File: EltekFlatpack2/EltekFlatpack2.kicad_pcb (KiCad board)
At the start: 2 copper layers, 26.2 x 81 mm, 14 parts

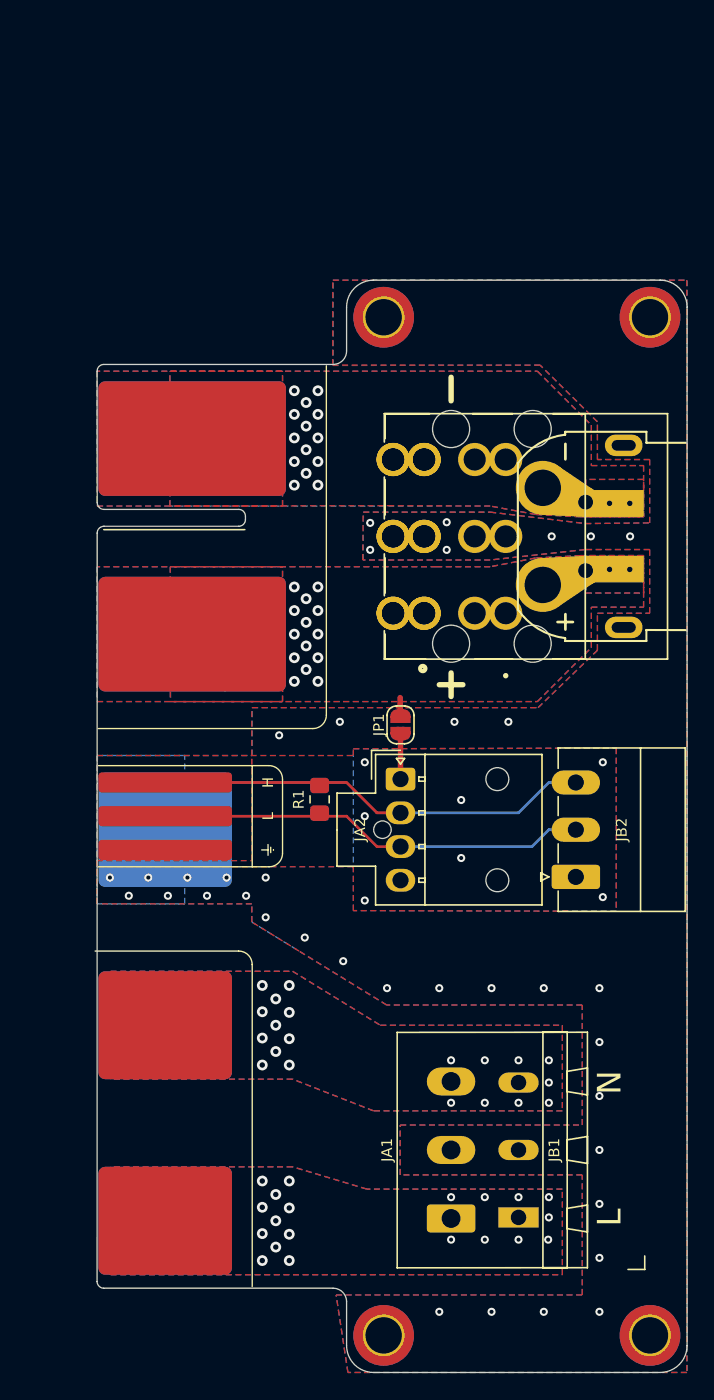
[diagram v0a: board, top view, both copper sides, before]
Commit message: fix makefile/panel/footprint (now has 1mm mill hole and straight edges!)
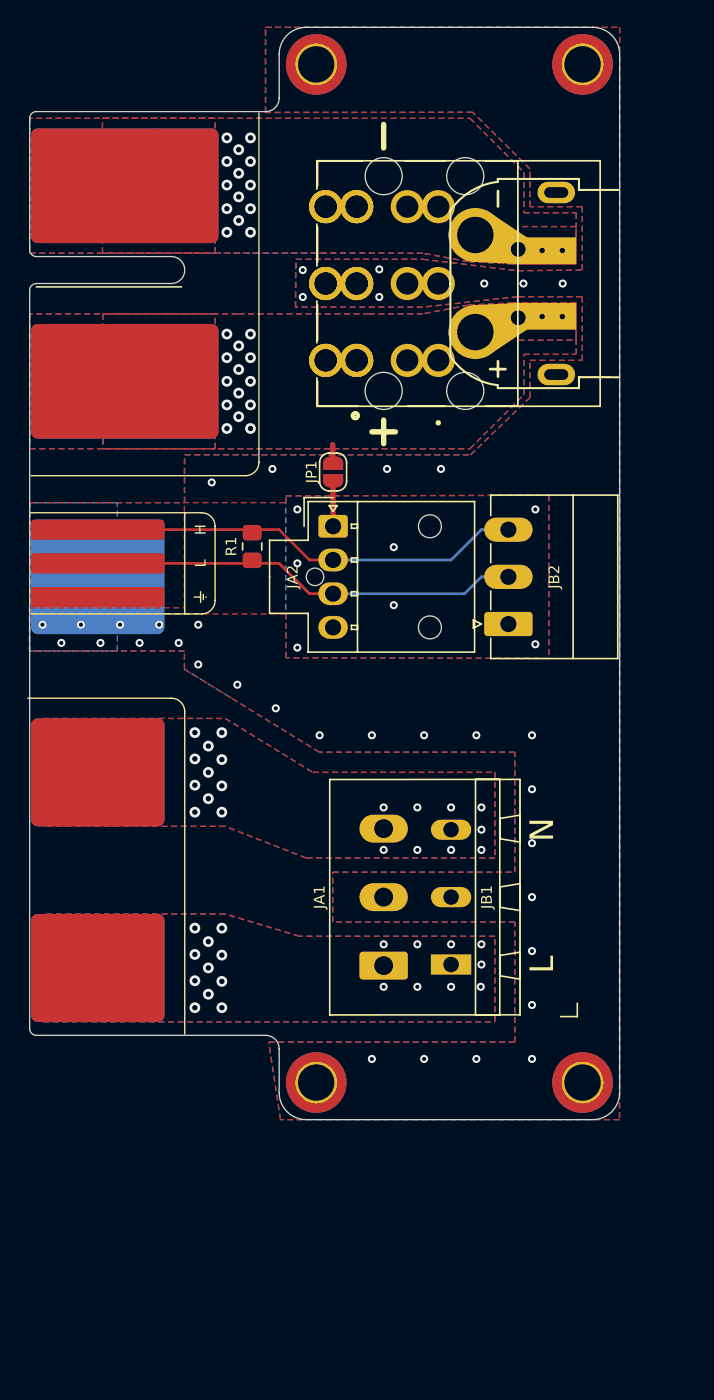
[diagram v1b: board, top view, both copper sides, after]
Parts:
- moved JA1 19.4 mm to (146.2, 119.6)
- moved H1 19.4 mm to (141.2, 128.2)
- moved H2 19.4 mm to (161.0, 128.2)
- moved H3 19.4 mm to (141.2, 52.8)
- moved H4 19.4 mm to (161.0, 52.8)
- moved JA2 19.4 mm to (142.5, 87.0)
- moved JA3 19.4 mm to (146.2, 69.0)
- moved JB1 19.4 mm to (151.2, 119.5)
- moved JB2 19.4 mm to (155.5, 94.2)
- moved JB3 19.4 mm to (152.3, 69.0)
- moved JC3 19.4 mm to (153.1, 69.0)
- moved JP1 19.4 mm to (142.5, 83.0)
- moved PC1 19.4 mm to (120.0, 56.2)
- moved R1 19.4 mm to (136.5, 88.5)
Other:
- board text removed: "appx 325mm to front of PSU"

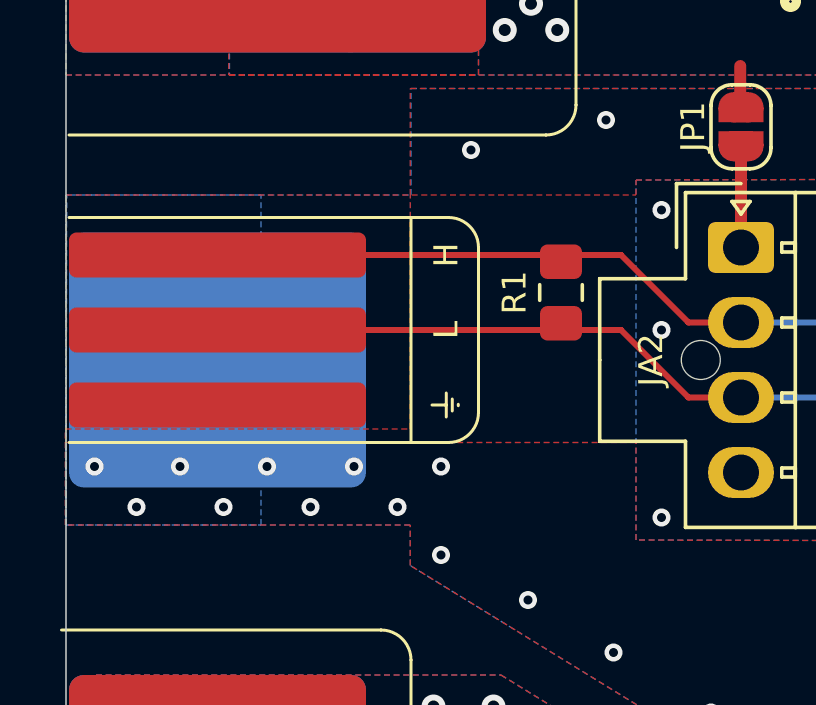
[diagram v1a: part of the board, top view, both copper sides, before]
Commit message: add THT termination resistor option
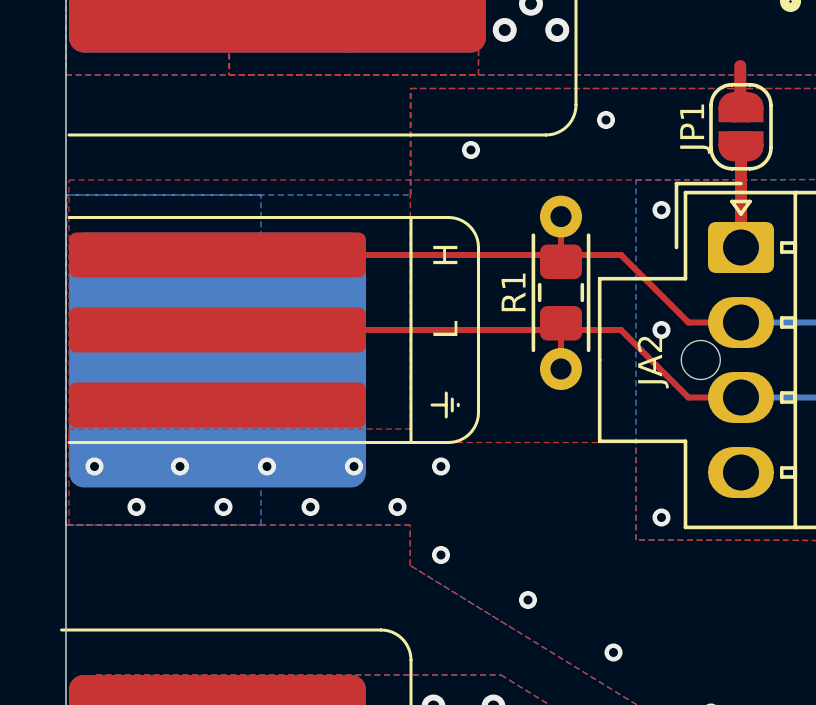
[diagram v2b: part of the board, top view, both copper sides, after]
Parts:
- added R2: 120R, Resistor_THT:R_Axial_DIN0204_L3.6mm_D1.6mm_P5.08mm_Horizontal, F.Cu at (136.5, 91.0)
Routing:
- net /CAN-: track 32.1 -> 33.7 mm
- net /CAN+: track 32.6 -> 34.1 mm
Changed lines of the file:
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@@
     (thickness 1.6)
     (drawings 32)
-    (tracks 140)
+    (tracks 142)
     (zones 0)
-    (modules 14)
+    (modules 15)
     (nets 10)
   )
@@
   )
   (setup
-    (last_trace_width 0.15)
+    (last_trace_width 0.2)
     (user_trace_width 0.15)
     (user_trace_width 0.2)
@@
     (add_net GNDD)
   )
+  (module Resistor_THT:R_Axial_DIN0204_L3.6mm_D1.6mm_P5.08mm_Horizontal (layer Front)
+    (at 136.5 91.05 90)
+    (descr "Resistor, Axial_DIN0204 series, Axial, Horizontal, pin pitch=5.08mm, 0.167W, length*diameter=3.6*1.6mm^2, http://cdn-reichelt.de/documents/datenblatt/B400/1_4W%23YAG.pdf")
+    (tags "Resistor Axial_DIN0204 series Axial Horizontal pin pitch 5.08mm 0.167W length 3.6mm diameter 1.6mm")
+    (fp_text reference R2 (at 2.54 -1.92 90) (layer F.SilkS) hide
+      (effects (font (size 1 1) (thickness 0.15)))
+    )
+    (fp_text value 120R (at 2.54 1.92 90) (layer F.Fab)
+      (effects (font (size 1 1) (thickness 0.15)))
+    )
+    (fp_line (start 6.03 -1.05) (end -0.95 -1.05) (layer F.CrtYd) (width 0.05))
+    (fp_line (start 6.03 1.05) (end 6.03 -1.05) (layer F.CrtYd) (width 0.05))
+    (fp_line (start -0.95 1.05) (end 6.03 1.05) (layer F.CrtYd) (width 0.05))
+    (fp_line (start -0.95 -1.05) (end -0.95 1.05) (layer F.CrtYd) (width 0.05))
+    (fp_line (start 0.62 0.92) (end 4.46 0.92) (layer F.SilkS) (width 0.12))
+    (fp_line (start 0.62 -0.92) (end 4.46 -0.92) (layer F.SilkS) (width 0.12))
+    (fp_line (start 5.08 0) (end 4.34 0) (layer F.Fab) (width 0.1))
+    (fp_line (start 0 0) (end 0.74 0) (layer F.Fab) (width 0.1))
+    (fp_line (start 4.34 -0.8) (end 0.74 -0.8) (layer F.Fab) (width 0.1))
+    (fp_line (start 4.34 0.8) (end 4.34 -0.8) (layer F.Fab) (width 0.1))
+    (fp_line (start 0.74 0.8) (end 4.34 0.8) (layer F.Fab) (width 0.1))
+    (fp_line (start 0.74 -0.8) (end 0.74 0.8) (layer F.Fab) (width 0.1))
+    (fp_text user %R (at 2.54 0 90) (layer F.Fab)
+      (effects (font (size 0.72 0.72) (thickness 0.108)))
+    )
+    (pad 2 thru_hole oval (at 5.08 0 90) (size 1.4 1.4) (drill 0.7) (layers *.Cu *.Mask)
+      (net 2 /CAN+))
+    (pad 1 thru_hole circle (at 0 0 90) (size 1.4 1.4) (drill 0.7) (layers *.Cu *.Mask)
+      (net 1 /CAN-))
+    (model ${KISYS3DMOD}/Resistor_THT.3dshapes/R_Axial_DIN0204_L3.6mm_D1.6mm_P5.08mm_Horizontal.wrl
+      (at (xyz 0 0 0))
+      (scale (xyz 1 1 1))
+      (rotate (xyz 0 0 0))
+    )
+  )
   (module EltekFlatpack2:CON_Edge_Flatpack2_AllContacts locked (layer Front)
     (at 120 56.25)
@@
       (effects (font (size 0.8 0.8) (thickness 0.12)))
     )
-    (fp_arc (start 10.5 11.75) (end 10.5 12.75) (angle -180) (layer Edge.Cuts) (width 0.05))
-    (fp_arc (start 0.5 13.25) (end 0.5 12.75) (angle -90) (layer Edge.Cuts) (width 0.05))
-    (fp_text user L (at 12.675 33.5 90 unlocked) (layer F.SilkS)
-      (effects (font (size 0.8 0.8) (thickness 0.12)))
-    )
-    (fp_arc (start 0.5 0.5) (end 0.5 0) (angle -90) (layer Edge.Cuts) (width 0.05))
-    (fp_arc (start 0.5 10.25) (end 0 10.25) (angle -90) (layer Edge.Cuts) (width 0.05))
-    (fp_arc (start 0.5 68) (end 0 68) (angle -90) (layer Edge.Cuts) (width 0.05))
-    (fp_arc (start 0.5 68) (end 0 68) (angle -90) (layer F.CrtYd) (width 0.05))
-    (fp_arc (start 0.5 0.5) (end 0.5 0) (angle -90) (layer F.CrtYd) (width 0.05))
-    (fp_arc (start 16 26) (end 16 27) (angle -90) (layer F.SilkS) (width 0.1))
-    (fp_text user H (at 12.675 31 90 unlocked) (layer F.SilkS)
-      (effects (font (size 0.8 0.8) (thickness 0.12)))
-    )
-    (fp_arc (start 12.75 30.75) (end 13.75 30.75) (angle -90) (layer F.SilkS) (width 0.1))
-    (fp_arc (start 12.75 36.25) (end 12.75 37.25) (angle -90) (layer F.SilkS) (width 0.1))
-    (fp_arc (start 10.5 44.5) (end 11.5 44.5) (angle -90) (layer F.SilkS) (width 0.1))
     (fp_line (start 13.75 30.75) (end 13.75 36.25) (layer F.SilkS) (width 0.1))
     (fp_line (start 0.1 37.25) (end 12.75 37.25) (layer F.SilkS) (width 0.1))
@@
     (fp_line (start 12.875 36.2) (end 12.875 35.8) (layer F.SilkS) (width 0.1))
     (fp_line (start 11.25 13) (end 0.5 13) (layer F.SilkS) (width 0.12))
+    (fp_arc (start 10.5 11.75) (end 10.5 12.75) (angle -180) (layer Edge.Cuts) (width 0.05))
+    (fp_arc (start 0.5 13.25) (end 0.5 12.75) (angle -90) (layer Edge.Cuts) (width 0.05))
+    (fp_text user L (at 12.675 33.5 90 unlocked) (layer F.SilkS)
+      (effects (font (size 0.8 0.8) (thickness 0.12)))
+    )
+    (fp_arc (start 0.5 0.5) (end 0.5 0) (angle -90) (layer Edge.Cuts) (width 0.05))
+    (fp_arc (start 0.5 10.25) (end 0 10.25) (angle -90) (layer Edge.Cuts) (width 0.05))
+    (fp_arc (start 0.5 68) (end 0 68) (angle -90) (layer Edge.Cuts) (width 0.05))
+    (fp_arc (start 0.5 68) (end 0 68) (angle -90) (layer F.CrtYd) (width 0.05))
+    (fp_arc (start 0.5 0.5) (end 0.5 0) (angle -90) (layer F.CrtYd) (width 0.05))
+    (fp_arc (start 16 26) (end 16 27) (angle -90) (layer F.SilkS) (width 0.1))
+    (fp_text user H (at 12.675 31 90 unlocked) (layer F.SilkS)
+      (effects (font (size 0.8 0.8) (thickness 0.12)))
+    )
+    (fp_arc (start 12.75 30.75) (end 13.75 30.75) (angle -90) (layer F.SilkS) (width 0.1))
+    (fp_arc (start 12.75 36.25) (end 12.75 37.25) (angle -90) (layer F.SilkS) (width 0.1))
+    (fp_arc (start 10.5 44.5) (end 11.5 44.5) (angle -90) (layer F.SilkS) (width 0.1))
     (pad CAN-L smd roundrect (at 5.05 33.5) (size 9.9 1.5) (layers Front F.Mask) (roundrect_rratio 0.167)
       (net 1 /CAN-) (solder_mask_margin 0.1016))
@@
   (segment (start 138.5 89.75) (end 140.75 92) (width 0.2) (layer Front) (net 1))
   (segment (start 136.45 89.75) (end 138.5 89.75) (width 0.2) (layer Front) (net 1))
+  (segment (start 136.5 89.525) (end 136.5 91.05) (width 0.2) (layer Front) (net 1))
   (segment (start 136.5 87.3) (end 136.55 87.25) (width 0.154) (layer Front) (net 2))
   (segment (start 136.5 87.475) (end 136.5 87.3) (width 0.154) (layer Front) (net 2))
@@
   (segment (start 151.25 89.5) (end 153.5 87.25) (width 0.2) (layer Back) (net 2))
   (segment (start 142.5 89.5) (end 151.25 89.5) (width 0.2) (layer Back) (net 2))
+  (segment (start 136.5 87.475) (end 136.5 85.97) (width 0.2) (layer Front) (net 2))
   (via (at 157.5 85.75) (size 0.6) (drill 0.3) (layers Front Back) (net 3))
   (via (at 157.5 95.75) (size 0.6) (drill 0.3) (layers Front Back) (net 3))
@@
         (xy 163.725 131) (xy 138.6 131) (xy 137.725 125.25) (xy 155.975 125.25) (xy 155.975 116.35)
         (xy 142.475 116.35) (xy 142.475 112.65) (xy 155.975 112.65) (xy 155.975 103.75) (xy 141.475 103.75)
-        (xy 134.975 99.75) (xy 131.475 97.6) (xy 131.475 96.25) (xy 119.975 96.25) (xy 119.975 93.05)
+        (xy 134.975 99.75) (xy 131.475 97.6) (xy 131.475 96.25) (xy 120.1 96.25) (xy 120.1 93.05)
         (xy 131.475 93.05) (xy 131.475 85.25) (xy 131.475 81.7) (xy 152.7 81.7) (xy 157.1 77.45)
         (xy 157.1 74.7) (xy 160.975 74.7) (xy 160.975 69.975) (xy 156.2 69.975) (xy 149.15 70.75)
@@
     (polygon
       (pts
-        (xy 158.5 96.8) (xy 139 96.75) (xy 139 93.5) (xy 120 93.5) (xy 120 85.25)
-        (xy 139 85.25) (xy 139 84.75) (xy 158.5 84.7)
-      )
-    )
+        (xy 158.5 96.8) (xy 139 96.75) (xy 139 93.5) (xy 120.1 93.5) (xy 120.1 84.75)
+        (xy 139 84.75) (xy 158.5 84.7)
+      )
+    )

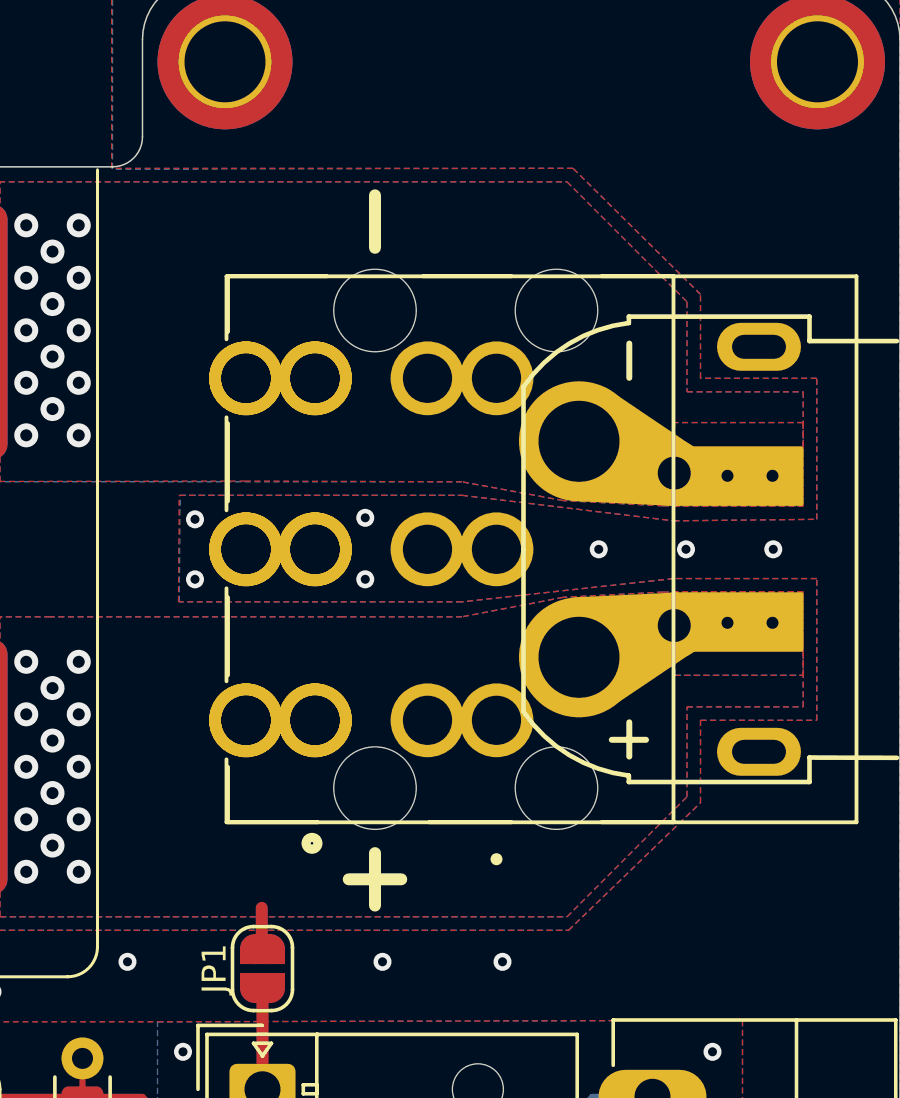
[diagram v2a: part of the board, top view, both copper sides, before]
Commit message: add keystone tab option
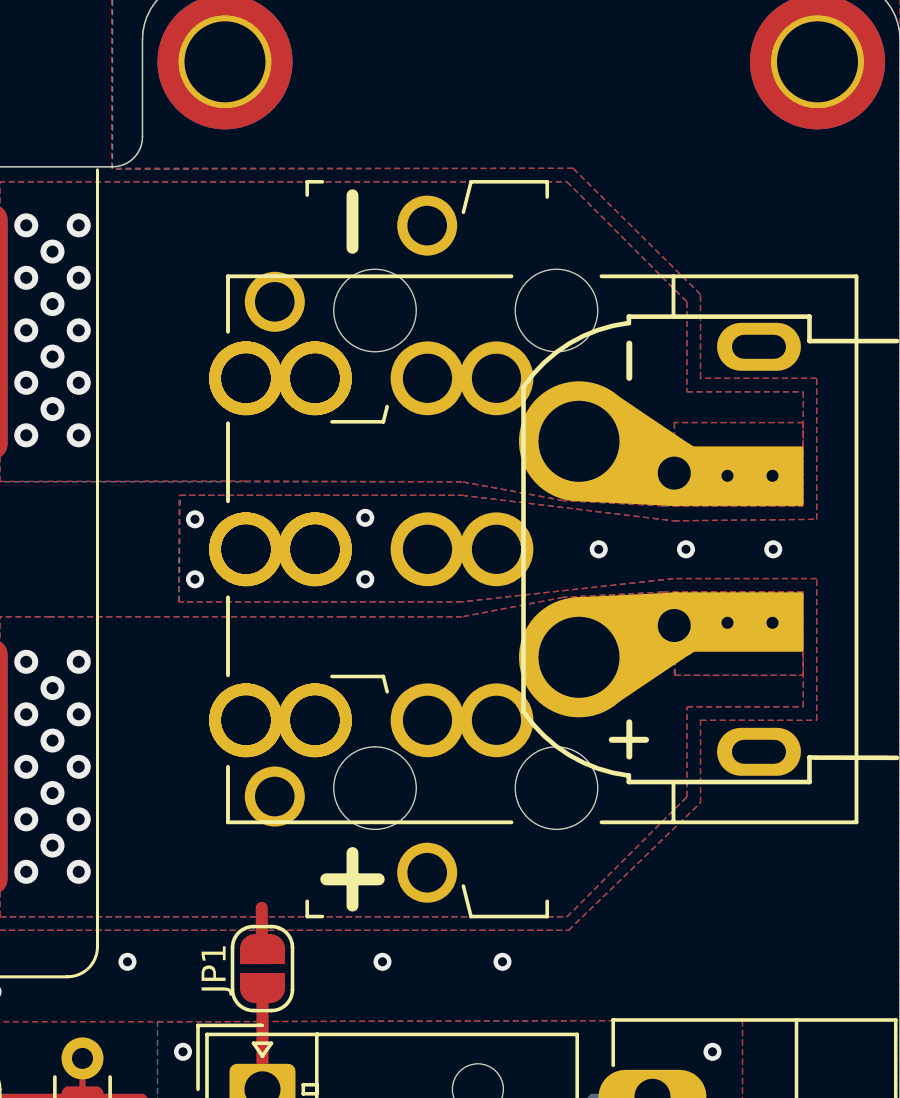
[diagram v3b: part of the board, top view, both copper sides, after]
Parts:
- added T1: Keystone 4912, 1 My Footprints:Connector_Keystone_4912_Overlaid, F.Cu at (145.4, 77.2)
- added T2: Keystone 4912, 1 My Footprints:Connector_Keystone_4912_Overlaid, F.Cu at (145.4, 60.8)
